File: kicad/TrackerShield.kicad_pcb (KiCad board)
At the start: 2 copper layers, 52.1 x 53.3 mm, 21 parts, among them P1 PWR_IN, P2 PWR_OUT, P3 MAIN_IO, P4 SECONDARY_IO, U1 Buck_Converter, U2 2N7002, U3 2N7002

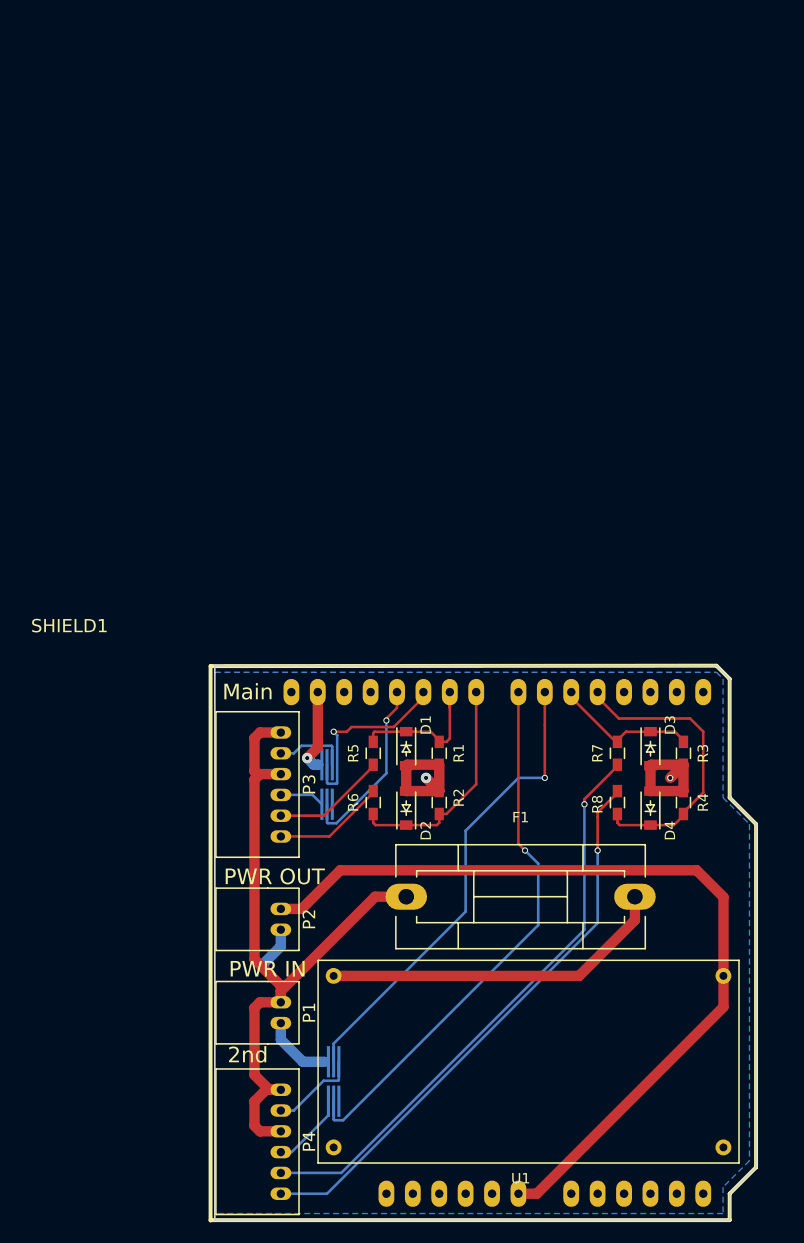
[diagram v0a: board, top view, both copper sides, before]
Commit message: Tested and failed to switch output FET.  Shield redesigned to provide transistor switching of FET.  Buck converter and fuse moved to allow internal antennas to be fitted without interference
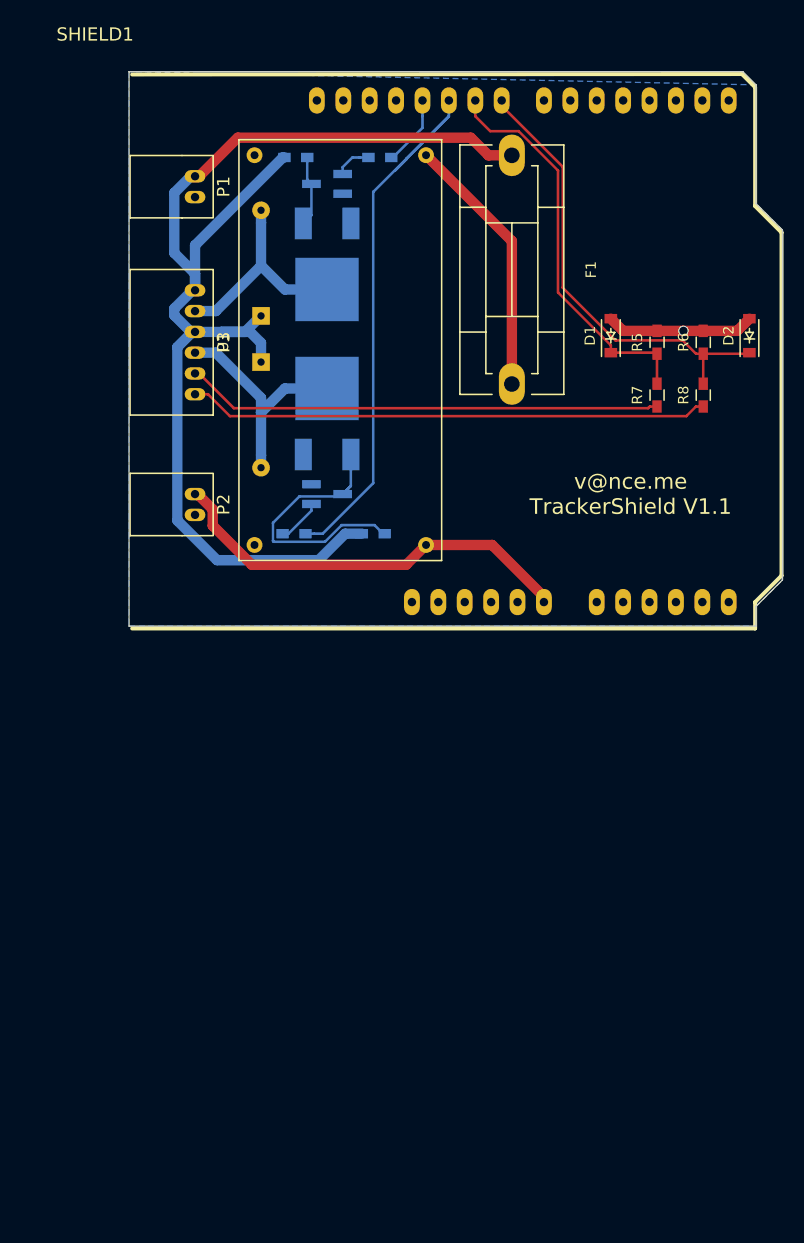
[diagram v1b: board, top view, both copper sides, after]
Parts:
- removed P4: SECONDARY_IO, JST-RA:JST-6RA
- removed U2, U3: 2N7002, SOT666:SOT666
- added Q1: BC848B, TO_SOT_Packages_SMD:SOT-23_Handsoldering, B.Cu at (173.4, 62.2)
- added Q2: Std12nf06lt4, TO_SOT_Packages_SMD:TO-252-2Lead, B.Cu at (173.4, 66.0)
- added Q3: BC848B, TO_SOT_Packages_SMD:SOT-23_Handsoldering, B.Cu at (173.4, 92.1)
- added Q4: Std12nf06lt4, TO_SOT_Packages_SMD:TO-252-2Lead, B.Cu at (173.4, 88.3)
- D3, D4: value 5.1V -> D; footprint Diodes_SMD:SOD-123 -> Diodes_ThroughHole:Diode_DO-35_SOD27_Horizontal_RM10; moved to B.Cu
- R1, R2, R3, R4: value 3k3 -> 10k; moved to B.Cu
- R5, R6: value 10k -> 3k3
- moved P1 79.9 mm to (160.7, 62.5)
- moved R2 63.6 mm to (170.3, 59.7), turned to 0 degrees
- moved U1 61.6 mm to (182.9, 77.5), turned to 270 degrees
- moved F1 60.3 mm to (191.1, 70.5), turned to 270 degrees
- moved R1 57.6 mm to (178.4, 59.7), turned to 0 degrees
- moved SHIELD1 57.0 mm to (148.5, 105.0)
- moved D4 57.0 mm to (167.0, 79.4), turned to 270 degrees
- moved D2 56.2 mm to (214.0, 76.8)
- moved D3 56.0 mm to (167.0, 74.9), turned to 90 degrees
- moved R6 54.5 mm to (209.6, 77.5), turned to 90 degrees
- moved R5 48.1 mm to (205.1, 77.5)
- moved D1 44.3 mm to (200.7, 76.8), turned to 90 degrees
- moved P3 43.3 mm to (160.7, 77.5)
- moved R3 43.0 mm to (170.2, 95.9), turned to 0 degrees
- moved P2 40.8 mm to (160.7, 93.1)
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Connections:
- D3 pad 2: GND -> Net-(D3-Pad2)
- D4 pad 1: Net-(D4-Pad1) -> Net-(D3-Pad1)
- D4 pad 2: GND -> Net-(D4-Pad2)
- F1 pad 1: Net-(F1-Pad1) -> Net-(D3-Pad1)
- P1 pad 1: Net-(F1-Pad1) -> Net-(D3-Pad1)
- P3 pad 1: Net-(F1-Pad1) -> Net-(D3-Pad1)
- P3 pad 2: Net-(P3-Pad2) -> Net-(D3-Pad2)
- P3 pad 3: Net-(F1-Pad1) -> Net-(D3-Pad1)
- P3 pad 4: Net-(P3-Pad4) -> Net-(D4-Pad2)
- R1 pad 1: Net-(D1-Pad1) -> Net-(Q1-Pad1)
- R1 pad 2: GND -> Net-(R1-Pad2)
- R2 pad 1: Net-(D2-Pad1) -> Net-(D3-Pad1)
- R2 pad 2: GND -> Net-(Q1-Pad3)
- R3 pad 1: Net-(D3-Pad1) -> Net-(Q3-Pad1)
- R3 pad 2: GND -> Net-(R3-Pad2)
- R4 pad 1: Net-(D4-Pad1) -> Net-(D3-Pad1)
- R4 pad 2: GND -> Net-(Q3-Pad3)
- R5 pad 1: Net-(P3-Pad5) -> Net-(D1-Pad1)
- R5 pad 2: Net-(D1-Pad1) -> GND
- R6 pad 1: Net-(P3-Pad6) -> Net-(D2-Pad1)
- R6 pad 2: Net-(D2-Pad1) -> GND
- R7 pad 1: Net-(P4-Pad5) -> Net-(P3-Pad5)
- R7 pad 2: Net-(D3-Pad1) -> Net-(D1-Pad1)
- R8 pad 1: Net-(P4-Pad6) -> Net-(P3-Pad6)
- R8 pad 2: Net-(D4-Pad1) -> Net-(D2-Pad1)
- SHIELD1 pad 10: Net-(SHIELD1-Pad10) -> Net-(R3-Pad2)
- SHIELD1 pad 11: Net-(SHIELD1-Pad11) -> Net-(R1-Pad2)
- SHIELD1 pad 4: Net-(D4-Pad1) -> Net-(SHIELD1-Pad4)
- SHIELD1 pad 5: Net-(D3-Pad1) -> Net-(SHIELD1-Pad5)
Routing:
- net Net-(D3-Pad1): track 14.1 -> 120.9 mm
- net Net-(F1-Pad1): track 69.6 -> 0.00 mm
- net Net-(P4-Pad5): track 56.1 -> 0.00 mm, vias 1 -> 0
- net Net-(R3-Pad2): track 0.00 -> 55.7 mm
- net Net-(P4-Pad6): track 54.8 -> 0.00 mm, vias 1 -> 0
- net Net-(SHIELD1-Pad7): track 52.4 -> 0.00 mm, vias 1 -> 0
- net Net-(SHIELD1-Pad6): track 45.5 -> 0.00 mm, vias 1 -> 0
- net +5VP: track 82.9 -> 40.7 mm
- net Net-(P3-Pad6): track 10.8 -> 50.2 mm
- net Net-(P3-Pad5): track 11.0 -> 45.9 mm
- net GND: track 45.4 -> 14.3 mm, vias 3 -> 1
- net Net-(D4-Pad1): track 28.6 -> 0.00 mm
- net Net-(Q3-Pad3): track 0.00 -> 26.6 mm
- net Net-(D1-Pad1): track 15.1 -> 38.6 mm
- net Net-(D4-Pad2): track 0.00 -> 22.2 mm
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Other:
- board size 52.1 x 53.3 mm -> 62.9 x 53.3 mm
- net class Power: via_drill 0.4 -> 0.8
- rule pad_to_mask_clearance: 0.2 -> 0
- board text added: "v@nce.me TrackerShield V1.1"
- board text removed: "2nd"
- board text removed: "Main"
- board text removed: "PWR IN"
- board text removed: "PWR OUT"
- board text removed: "TrackerShield v1.0"
- board text removed: "v@nce.me"

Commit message: Redesigned board submitted for manufacture
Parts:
- added D10: LED, SMD_LED:LED_SMD_1.6x0.8mm, F.Cu at (206.4, 60.3)
- added D11: LED, SMD_LED:LED_SMD_1.6x0.8mm, F.Cu at (204.5, 60.3)
- added D12: LED, SMD_LED:LED_SMD_1.6x0.8mm, F.Cu at (202.6, 60.3)
- added D13: LED, SMD_LED:LED_SMD_1.6x0.8mm, F.Cu at (200.7, 60.3)
- added D14: LED, SMD_LED:LED_SMD_1.6x0.8mm, F.Cu at (198.8, 60.3)
- added D5: LED, SMD_LED:LED_SMD_1.6x0.8mm, F.Cu at (157.5, 67.9)
- added D6: LED, SMD_LED:LED_SMD_1.6x0.8mm, F.Cu at (157.5, 87.6)
- added D7: LED, SMD_LED:LED_SMD_1.6x0.8mm, F.Cu at (212.1, 60.3)
- added D8: LED, SMD_LED:LED_SMD_1.6x0.8mm, F.Cu at (210.2, 60.3)
- added D9: LED, SMD_LED:LED_SMD_1.6x0.8mm, F.Cu at (208.3, 60.3)
- added R10: 220, Resistors_SMD:R_0603_HandSoldering, F.Cu at (161.9, 87.6)
- added R11: 220, Resistors_SMD:R_0603_HandSoldering, F.Cu at (212.1, 64.6)
- added R12: 220, Resistors_SMD:R_0603_HandSoldering, F.Cu at (210.2, 64.6)
- added R13: 220, Resistors_SMD:R_0603_HandSoldering, F.Cu at (208.3, 64.6)
- added R14: 220, Resistors_SMD:R_0603_HandSoldering, F.Cu at (206.4, 64.6)
- added R15: 220, Resistors_SMD:R_0603_HandSoldering, F.Cu at (204.5, 64.6)
- added R16: 220, Resistors_SMD:R_0603_HandSoldering, F.Cu at (202.6, 64.6)
- added R17: 220, Resistors_SMD:R_0603_HandSoldering, F.Cu at (200.7, 64.6)
- added R18: 220, Resistors_SMD:R_0603_HandSoldering, F.Cu at (198.8, 64.6)
- added R9: 220, Resistors_SMD:R_0603_HandSoldering, F.Cu at (161.9, 67.9)
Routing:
- net GND: track 14.3 -> 68.9 mm, vias 1 -> 5
- net +5VP: track 40.7 -> 66.7 mm
- net Net-(R3-Pad2): track 55.7 -> 48.4 mm
- net Net-(D14-Pad2): track 0.00 -> 6.83 mm
- net Net-(D13-Pad2): track 0.00 -> 6.44 mm
- net Net-(D12-Pad2): track 0.00 -> 6.38 mm
- net Net-(D11-Pad2): track 0.00 -> 6.12 mm
- net Net-(D10-Pad2): track 0.00 -> 5.85 mm
- net Net-(D9-Pad2): track 0.00 -> 5.59 mm
- net Net-(D3-Pad2): track 20.8 -> 26.1 mm
- net Net-(D8-Pad2): track 0.00 -> 5.12 mm
- net Net-(D7-Pad2): track 0.00 -> 4.86 mm
- net Net-(D4-Pad2): track 22.2 -> 26.9 mm
- net Net-(D6-Pad1): track 0.00 -> 2.04 mm
- net Net-(D5-Pad1): track 0.00 -> 2.04 mm
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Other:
- board text added: "0"
- board text added: "1"
- board text added: "2"
- board text added: "3"
- board text added: "4"
- board text added: "5"
- board text added: "6"
- board text added: "7"
